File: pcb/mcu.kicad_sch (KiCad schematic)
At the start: 19 parts, among them J1 AVR-UPDI-6, U1 ATtiny1616-MNR

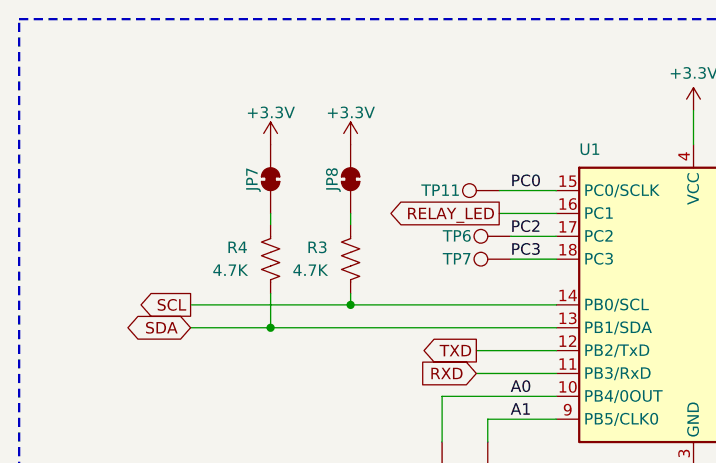
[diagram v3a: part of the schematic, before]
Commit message: Updated I2C pulls to open jumper
Fixed I2C to be open rather than bridged.
Changed opto-isolator to CRGM library.
Updated picture of bottom side to match new footprint
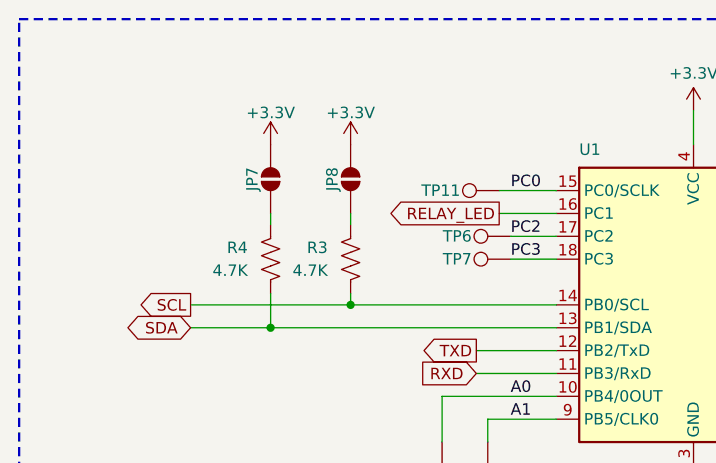
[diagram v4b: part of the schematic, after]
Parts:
- JP7, JP8: footprint CRGM Connector:SolderJumper-2_P1.3mm_Bridged_RoundedPad1.0x1.5mm -> CRGM Connector:SolderJumper-2_P1.3mm_Open_RoundedPad1.0x1.5mm; symbol Jumper:SolderJumper_2_Bridged -> CRGM Connector:SolderJumper_2_Open
- TP10, TP11, TP12, TP13, TP14, TP3, TP6, TP7, TP8, TP9: now left out of the parts list
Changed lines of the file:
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@@
+			)
+		)
+		(property "Sim.Enable" ""
+			(at 72.39 76.2 0)
+			(effects
+				(font
+					(size 1.27 1.27)
+				)
+				(hide yes)
 			)
 		)
@@
 		(unit 1)
 		(exclude_from_sim no)
-		(in_bom yes)
+		(in_bom no)
 		(on_board yes)
 		(dnp no)
@@
 			)
 		)
+		(property "Sim.Enable" ""
+			(at 80.01 52.07 90)
+			(effects
+				(font
+					(size 1.27 1.27)
+				)
+				(hide yes)
+			)
+		)
 		(pin "1"
 		)
@@
 		(unit 1)
 		(exclude_from_sim no)
-		(in_bom yes)
+		(in_bom no)
 		(on_board yes)
 		(dnp no)
@@
 			)
 		)
+		(property "Sim.Enable" ""
+			(at 121.92 57.15 90)
+			(effects
+				(font
+					(size 1.27 1.27)
+				)
+				(hide yes)
+			)
+		)
 		(pin "1"
 		)
@@
 		(unit 1)
 		(exclude_from_sim no)
-		(in_bom yes)
+		(in_bom no)
 		(on_board yes)
 		(dnp no)
@@
 		(property "Description" "Test Point D1.0mm"
 			(at 89.154 49.53 0)
+			(effects
+				(font
+					(size 1.27 1.27)
+				)
+				(hide yes)
+			)
+		)
+		(property "Sim.Enable" ""
+			(at 80.01 49.53 90)
 			(effects
 				(font
@@
 			)
 		)
+		(property "Sim.Enable" ""
+			(at 187.96 45.72 0)
+			(effects
+				(font
+					(size 1.27 1.27)
+				)
+				(hide yes)
+			)
+		)
 		(pin "4"
 		)
@@
 			)
 		)
+		(property "Sim.Enable" ""
+			(at 128.27 87.63 0)
+			(effects
+				(font
+					(size 1.27 1.27)
+				)
+				(hide yes)
+			)
+		)
 		(pin "1"
 		)
@@
 		(unit 1)
 		(exclude_from_sim no)
-		(in_bom yes)
+		(in_bom no)
 		(on_board yes)
 		(dnp no)
@@
 		(property "Description" "Test Point D1.0mm"
 			(at 175.26 47.244 0)
+			(effects
+				(font
+					(size 1.27 1.27)
+				)
+				(hide yes)
+			)
+		)
+		(property "Sim.Enable" ""
+			(at 175.26 38.1 0)
 			(effects
 				(font
@@
 			)
 		)
+		(property "Sim.Enable" ""
+			(at 62.23 52.07 0)
+			(effects
+				(font
+					(size 1.27 1.27)
+				)
+				(hide yes)
+			)
+		)
 		(pin "2"
 		)
@@
 		(unit 1)
 		(exclude_from_sim no)
-		(in_bom yes)
+		(in_bom no)
 		(on_board yes)
 		(dnp no)
@@
 		(property "Description" "Test Point D1.0mm"
 			(at 112.776 46.99 0)
+			(effects
+				(font
+					(size 1.27 1.27)
+				)
+				(hide yes)
+			)
+		)
+		(property "Sim.Enable" ""
+			(at 121.92 46.99 90)
 			(effects
 				(font
@@
 			)
 		)
+		(property "Sim.Enable" ""
+			(at 53.34 52.07 0)
+			(effects
+				(font
+					(size 1.27 1.27)
+				)
+				(hide yes)
+			)
+		)
 		(pin "2"
 		)
@@
 		(unit 1)
 		(exclude_from_sim no)
-		(in_bom yes)
+		(in_bom no)
 		(on_board yes)
 		(dnp no)
@@
 			)
 		)
+		(property "Sim.Enable" ""
+			(at 121.92 49.53 90)
+			(effects
+				(font
+					(size 1.27 1.27)
+				)
+				(hide yes)
+			)
+		)
 		(pin "1"
 		)
@@
 	)
 	(symbol
-		(lib_id "Jumper:SolderJumper_2_Bridged")
+		(lib_id "CRGM Connector:SolderJumper_2_Open")
 		(at 62.23 43.18 90)
 		(unit 1)
@@
 			)
 		)
-		(property "Footprint" "CRGM Connector:SolderJumper-2_P1.3mm_Bridged_RoundedPad1.0x1.5mm"
-			(at 62.23 43.18 0)
+		(property "Footprint" "CRGM Connector:SolderJumper-2_P1.3mm_Open_RoundedPad1.0x1.5mm"
+			(at 72.644 43.18 0)
 			(effects
 				(font
@@
 		)
 		(property "Datasheet" "~"
-			(at 62.23 43.18 0)
-			(effects
-				(font
-					(size 1.27 1.27)
-				)
-				(hide yes)
-			)
-		)
-		(property "Description" "Solder Jumper, 2-pole, closed/bridged"
-			(at 62.23 43.18 0)
+			(at 70.358 43.18 0)
+			(effects
+				(font
+					(size 1.27 1.27)
+				)
+				(hide yes)
+			)
+		)
+		(property "Description" "Solder Jumper, 2-pole, open"
+			(at 67.564 43.18 0)
 			(effects
 				(font
@@
 			)
 		)
+		(property "Sim.Enable" ""
+			(at 62.23 43.18 0)
+			(effects
+				(font
+					(size 1.27 1.27)
+				)
+				(hide yes)
+			)
+		)
 		(pin "2"
 		)
@@
 		(unit 1)
 		(exclude_from_sim no)
-		(in_bom yes)
+		(in_bom no)
 		(on_board yes)
 		(dnp no)
@@
 		(property "Description" "Test Point D1.0mm"
 			(at 87.884 44.45 0)
+			(effects
+				(font
+					(size 1.27 1.27)
+				)
+				(hide yes)
+			)
+		)
+		(property "Sim.Enable" ""
+			(at 78.74 44.45 90)
 			(effects
 				(font
@@
 	)
 	(symbol
-		(lib_id "Jumper:SolderJumper_2_Bridged")
+		(lib_id "CRGM Connector:SolderJumper_2_Open")
 		(at 53.34 43.18 90)
 		(unit 1)
@@
 			)
 		)
-		(property "Footprint" "CRGM Connector:SolderJumper-2_P1.3mm_Bridged_RoundedPad1.0x1.5mm"
-			(at 53.34 43.18 0)
+		(property "Footprint" "CRGM Connector:SolderJumper-2_P1.3mm_Open_RoundedPad1.0x1.5mm"
+			(at 63.754 43.18 0)
 			(effects
 				(font
@@
 		)
 		(property "Datasheet" "~"
-			(at 53.34 43.18 0)
-			(effects
-				(font
-					(size 1.27 1.27)
-				)
-				(hide yes)
-			)
-		)
-		(property "Description" "Solder Jumper, 2-pole, closed/bridged"
-			(at 53.34 43.18 0)
+			(at 61.468 43.18 0)
+			(effects
+				(font
+					(size 1.27 1.27)
+				)
+				(hide yes)
+			)
+		)
+		(property "Description" "Solder Jumper, 2-pole, open"
+			(at 58.674 43.18 0)
 			(effects
 				(font
@@
 			)
 		)
+		(property "Sim.Enable" ""
+			(at 53.34 43.18 0)
+			(effects
+				(font
+					(size 1.27 1.27)
+				)
+				(hide yes)
+			)
+		)
 		(pin "2"
 		)
@@
 		(unit 1)
 		(exclude_from_sim no)
-		(in_bom yes)
+		(in_bom no)
 		(on_board yes)
 		(dnp no)
@@
 			)
 		)
+		(property "Sim.Enable" ""
+			(at 121.92 62.23 90)
+			(effects
+				(font
+					(size 1.27 1.27)
+				)
+				(hide yes)
+			)
+		)
 		(pin "1"
 		)
@@
 		(unit 1)
 		(exclude_from_sim no)
-		(in_bom yes)
+		(in_bom no)
 		(on_board yes)
 		(dnp no)
@@
 			)
 		)
+		(property "Sim.Enable" ""
+			(at 121.92 52.07 90)
+			(effects
+				(font
+					(size 1.27 1.27)
+				)
+				(hide yes)
+			)
+		)
 		(pin "1"
 		)
@@
 		(unit 1)
 		(exclude_from_sim no)
-		(in_bom yes)
+		(in_bom no)
 		(on_board yes)
 		(dnp no)
@@
 			)
 		)
+		(property "Sim.Enable" ""
+			(at 121.92 59.69 90)
+			(effects
+				(font
+					(size 1.27 1.27)
+				)
+				(hide yes)
+			)
+		)
 		(pin "1"
 		)
@@
 			)
 		)
+		(property "Sim.Enable" ""
+			(at 100.33 62.23 0)
+			(effects
+				(font
+					(size 1.27 1.27)
+				)
+				(hide yes)
+			)
+		)
 		(pin "21"
 		)
@@
 			(at 77.47 76.2 0)
 			(effects
+				(font
+					(size 1.27 1.27)
+				)
+				(hide yes)
+			)
+		)
+		(property "Sim.Enable" ""
+			(at 77.47 76.2 0)
+			(effects

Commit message: Updated for consistency with new patterns
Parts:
- removed J1: AVR-UPDI-6, CRGM Connector:PinHeader_2x03_P2.54mm_Vertical_SMD, symbol CRGM Connector:AVR-UPDI-6
- added J1: AVR-UPDI-UART-6, CRGM Connector:PinHeader_2x03_P2.54mm_Vertical_SMD, symbol CRGM Connector:AVR-UPDI-UART-6
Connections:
- net +3.3V: now also J1.2 (VCC)
- net GND: now also J1.6 (GND)
- net RXD: now also J1.4 (RXD)
- net TXD: now also J1.5 (TXD)
- net UPDI: now also J1.1 (DATA)
